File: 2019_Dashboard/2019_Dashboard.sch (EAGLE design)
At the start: 61 parts, among them IC1 MCP23017SO, Q1 TN0602N3, Q2 TN0602N3, Q3 TN0602N3, Q4 TN0602N3, Q5 TN0602N3, U1 TLC59281, Y1 16MHz

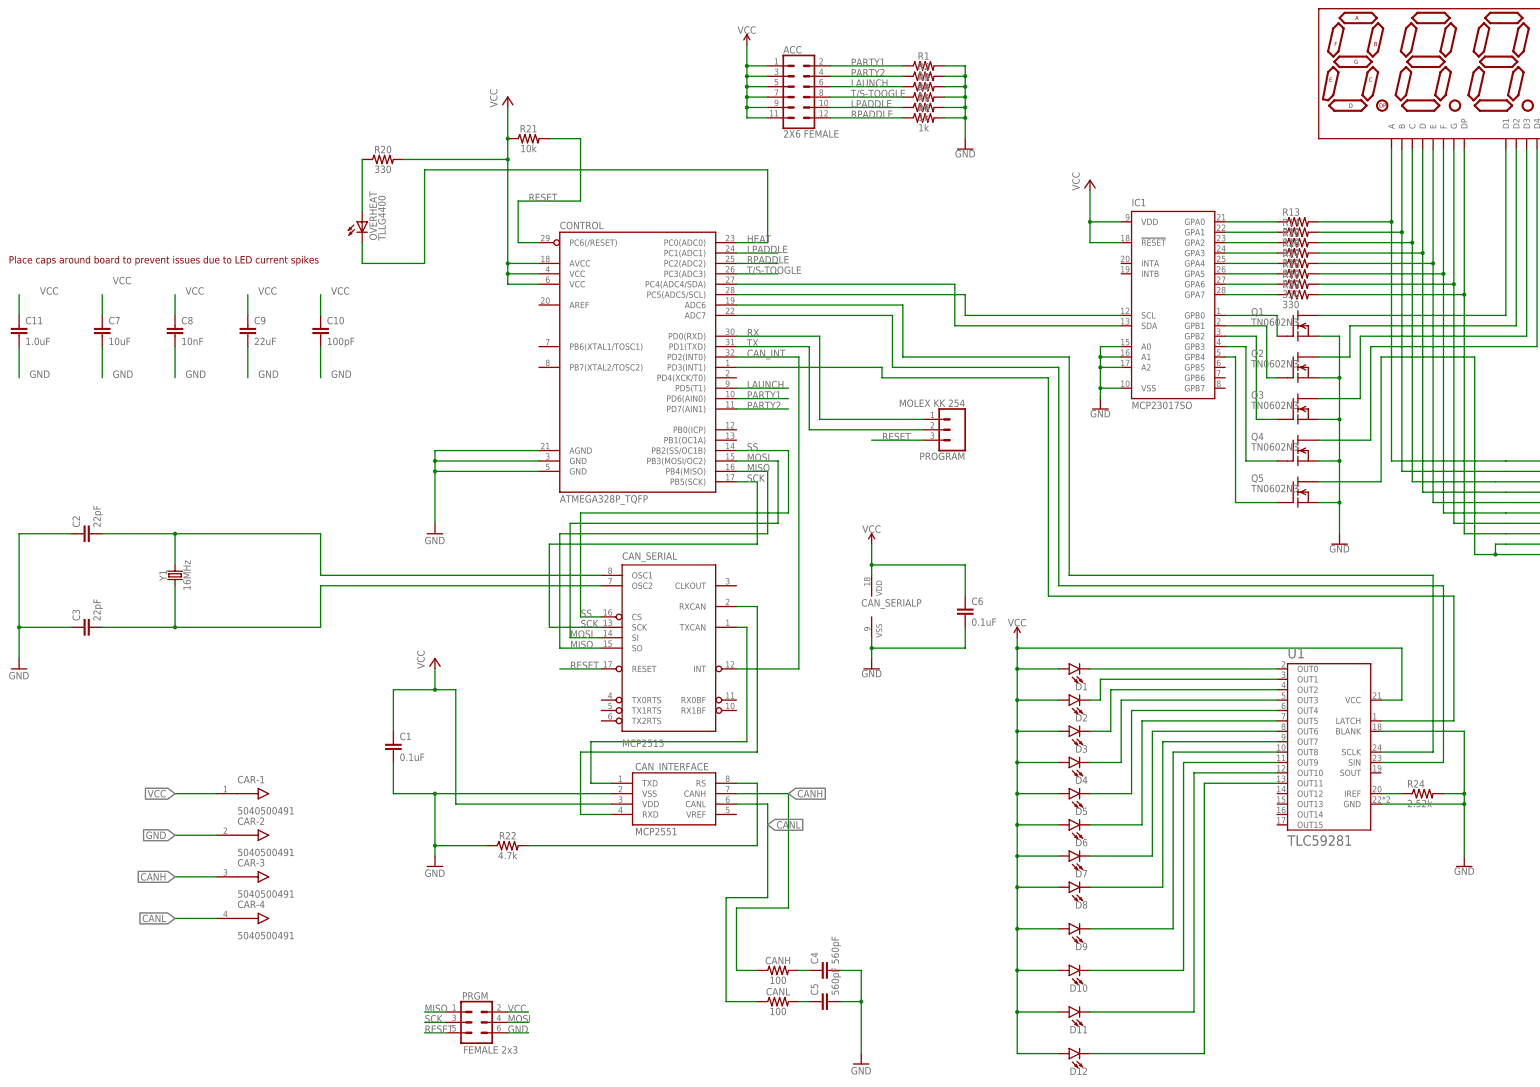
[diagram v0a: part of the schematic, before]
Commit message: Updated dashboard schematic, fix post-order bugs
Board not updated yet
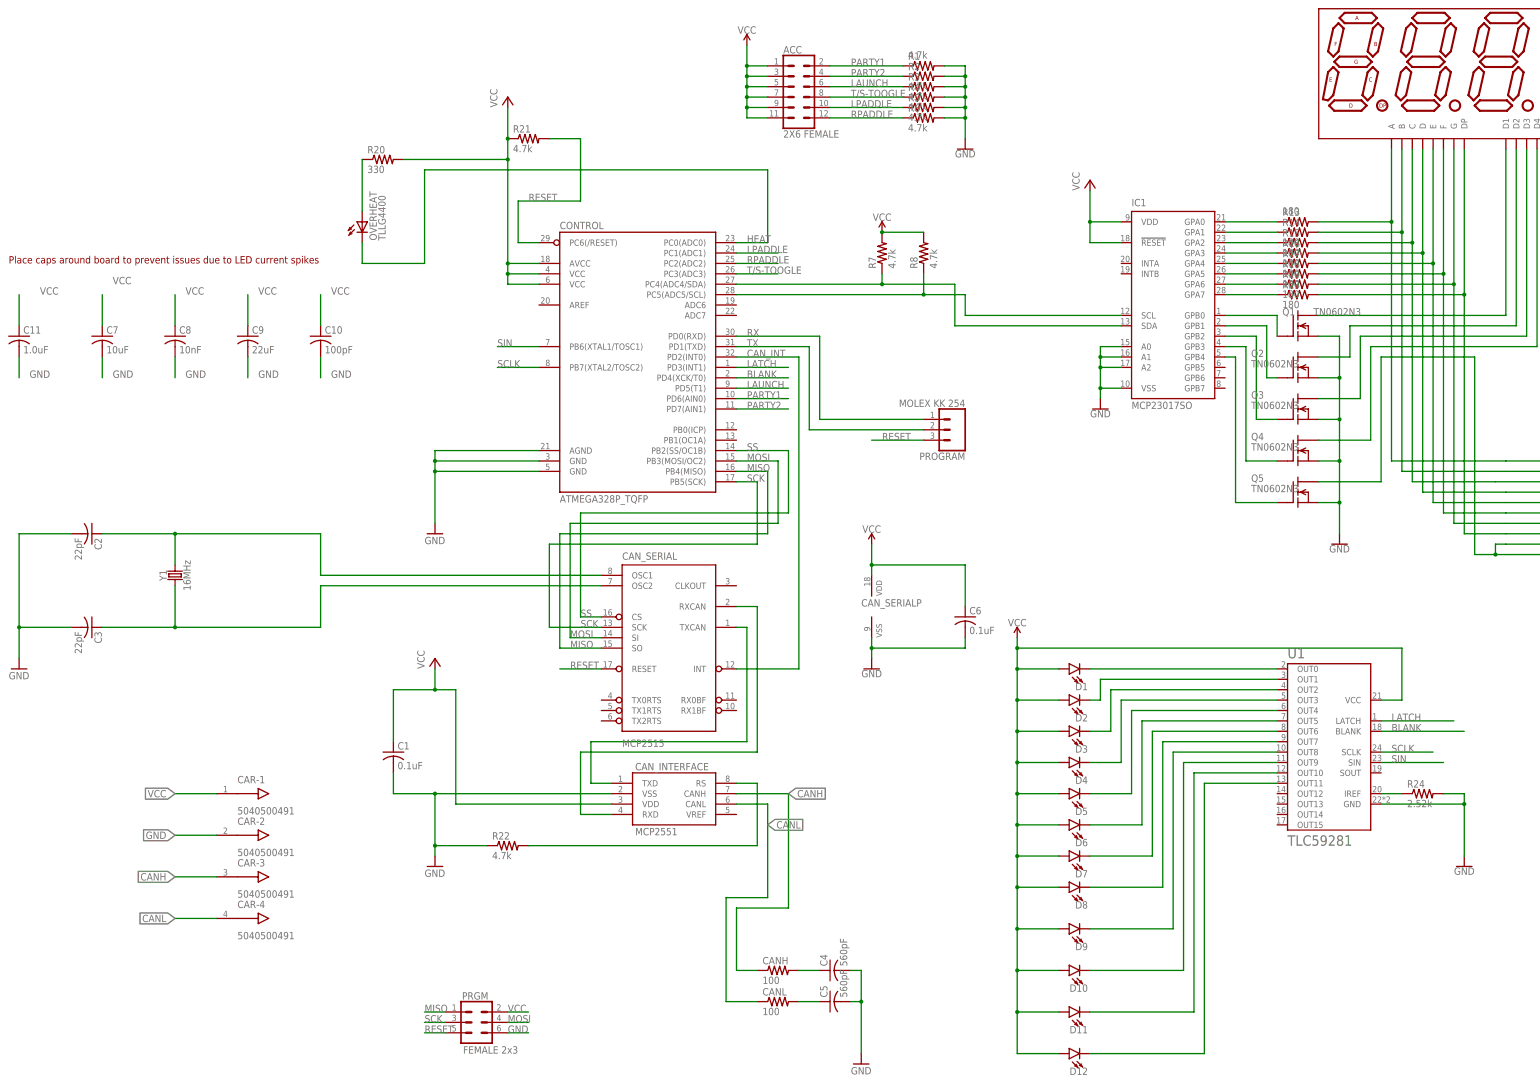
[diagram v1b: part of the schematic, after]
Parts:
- added R7, R8: 4.7k, rcl:R-US_R0603
- C1: device SparkFun-Capacitors:0.1UF-0603-25V-(+80/-20%) -> rcl:C-USC0603
- C10: device SparkFun-Capacitors:100PF-0603-50V-5% -> rcl:C-USC0603
- C11: device SparkFun-Capacitors:1.0UF-0805-25V-(+80/-20%) -> rcl:C-USC0603
- C2, C3: device SparkFun-Capacitors:22PF-0603-50V-5% -> rcl:C-USC0603
- C4, C5: device SparkFun-Capacitors:560PF-0603-50V-5% -> rcl:C-USC0603
- C6: device SparkFun-Capacitors:0.1UF-0402-16V-10% -> rcl:C-USC0603
- C7: device SparkFun-Capacitors:10UF-0805-10V-10% -> rcl:C-USC0603
- C8: device SparkFun-Capacitors:10NF-0603-50V-10% -> rcl:C-USC0603
- C9: device SparkFun-Capacitors:22UF-0805-6.3V-20% -> rcl:C-USC0603
- CANH, CANL: device SparkFun-Resistors:100OHM-0603-1/4W-5% -> rcl:R-US_R0603
- R1, R2, R3, R4, R5, R6: value 1k -> 4.7k; device SparkFun-Resistors:1KOHM-0603-1/10W-1% -> rcl:R-US_R0603
- R13, R14, R16, R17, R18, R19, R23: value 330 -> 180; device resistor:R-US_R0603 -> rcl:R-US_R0603
- R15: value 330 -> 180\; device resistor:R-US_R0603 -> rcl:R-US_R0603
- R20: device SparkFun-Resistors:330OHM-0603-1/10W-1% -> rcl:R-US_R0603
- R21: value 10k -> 4.7k; device SparkFun-Resistors:10KOHM-0603-1/10W-1% -> rcl:R-US_R0603
- R22: device SparkFun-Resistors:4.7KOHM-0603-1/10W-1% -> rcl:R-US_R0603
- R24: device resistor:R-US_R0603 -> rcl:R-US_R0603
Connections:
- net N$20 renamed LATCH
- removed net N$18: CONTROL.ADC6, U1.SCLK
- removed net N$19: CONTROL.ADC7, U1.SIN
- new net BLANK: CONTROL.PD4(XCK/T0), U1.BLANK
- new net SCLK: CONTROL.PB7(XTAL2/TOSC2), U1.SCLK
- new net SIN: CONTROL.PB6(XTAL1/TOSC1), U1.SIN
- net GND: now also C2.2, C3.2; no longer C2.1, C3.1, U1.BLANK
- net N$1: now also R8.1
- net N$2: now also R7.1
- net OSC1: now also C2.1; no longer C2.2
- net OSC2: now also C3.1; no longer C3.2
- net VCC: now also R7.2, R8.2
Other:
- moved on the sheet: C1, C10, C11, C2, C3, C4, C5, C6, C7, C8, C9
